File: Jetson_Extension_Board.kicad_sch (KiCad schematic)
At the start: 8 parts, among them J6 40_Pin_Jetson_Connector, SW1 SW_Push_DPDT

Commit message: PCB Update
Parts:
- added J14: Conn_01x06_Pin, Connector_JST:JST_EH_B6B-EH-A_1x06_P2.50mm_Vertical, symbol Connector:Conn_01x06_Pin
- added J15: Conn_01x04_Pin, Connector_JST:JST_EH_B4B-EH-A_1x04_P2.50mm_Vertical, symbol Connector:Conn_01x04_Pin
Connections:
- net 3.3V: now also SW1.3 (C); no longer SW1.1 (A)
- net ADC/3.3V: now also J14.5 (Pin_5), J14.6 (Pin_6)
- net COM 3: now also J15.1 (Pin_1)
- net GND: now also SW1.1 (A), J14.4 (Pin_4), J15.3 (Pin_3), J15.4 (Pin_4); no longer SW1.3 (C)
- net I2C_2_SCL: now also J14.2 (Pin_2)
- net I2C_2_SDA: now also J14.3 (Pin_3)
- net IMU INT: now also J15.2 (Pin_2)
- net IMU nRESET: now also J14.1 (Pin_1)
- net IMU nBOOT: no longer names the net of J6.33 (Pin_33)
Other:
- removed sheet IMU(BN0055)

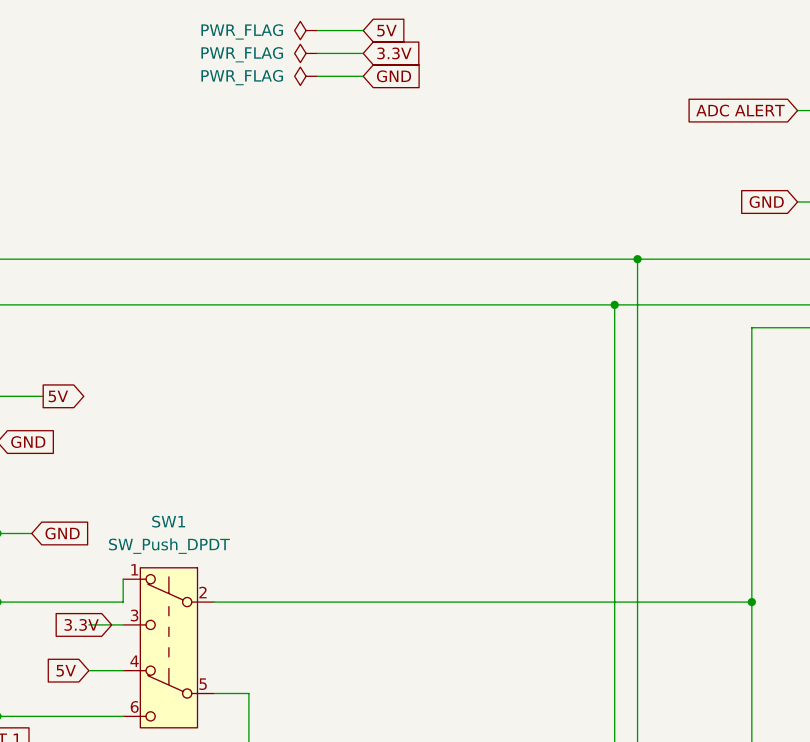
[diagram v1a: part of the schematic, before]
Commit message: added connectors for pots and compacted further
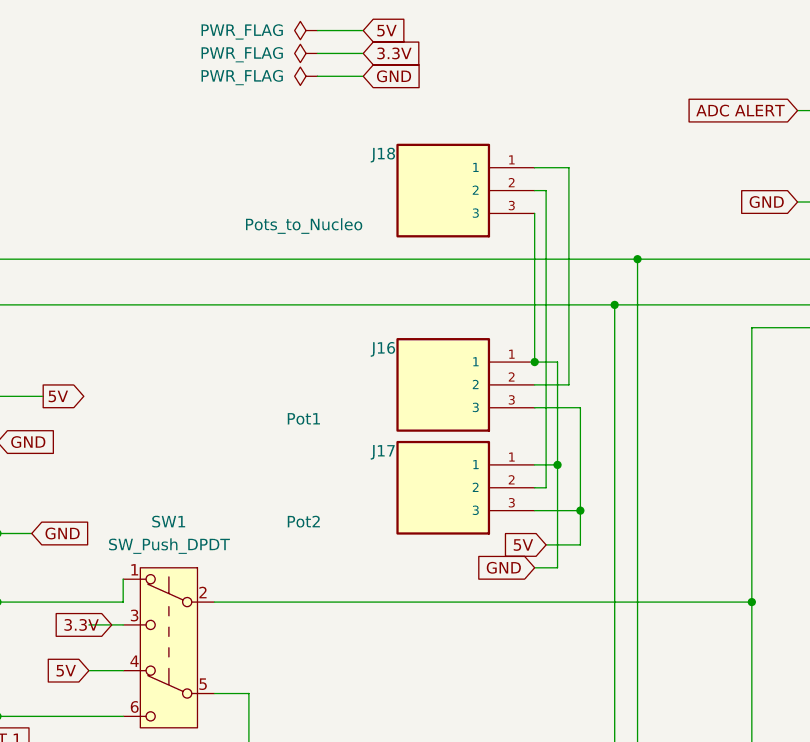
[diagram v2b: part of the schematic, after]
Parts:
- added J16: Pot1, TBP03R2_350_03BE(1):CUI_TBP03R2-350-03BE, symbol TBP03R2-350-03BE:TBP03R2-350-03BE
- added J17: Pot2, TBP03R2_350_03BE(1):CUI_TBP03R2-350-03BE, symbol TBP03R2-350-03BE:TBP03R2-350-03BE
- added J18: Pots_to_Nucleo, TBP03R2_350_03BE(1):CUI_TBP03R2-350-03BE, symbol TBP03R2-350-03BE:TBP03R2-350-03BE
- J14: footprint Connector_JST:JST_EH_B6B-EH-A_1x06_P2.50mm_Vertical -> Connector_PinSocket_2.54mm:PinSocket_1x06_P2.54mm_Vertical
- J15: footprint Connector_JST:JST_EH_B4B-EH-A_1x04_P2.50mm_Vertical -> Connector_PinSocket_2.54mm:PinSocket_1x04_P2.54mm_Vertical
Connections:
- net 5V: now also J16.3, J17.3
- net GND: now also J16.1, J17.1, J18.3
- new net: J17.2, J18.2
- new net: J16.2, J18.1

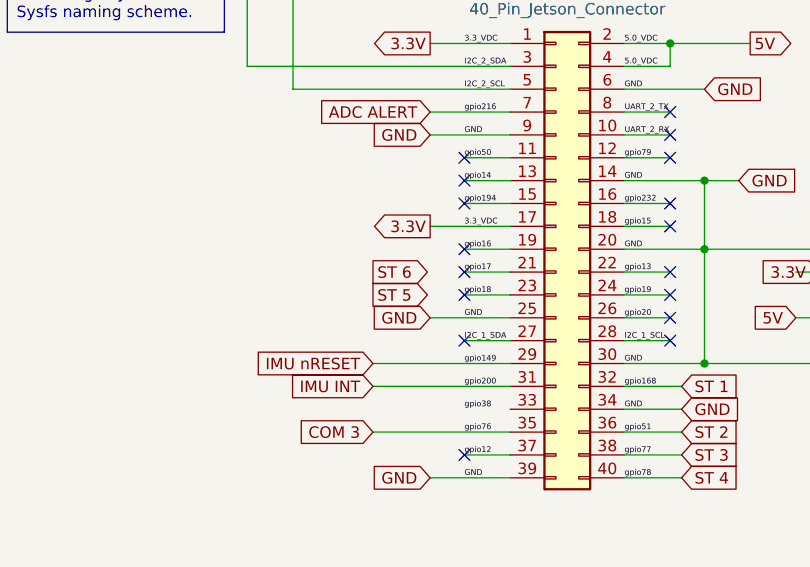
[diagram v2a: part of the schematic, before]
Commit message: changed hole sizes, added labels, added ground plane, set trace width min
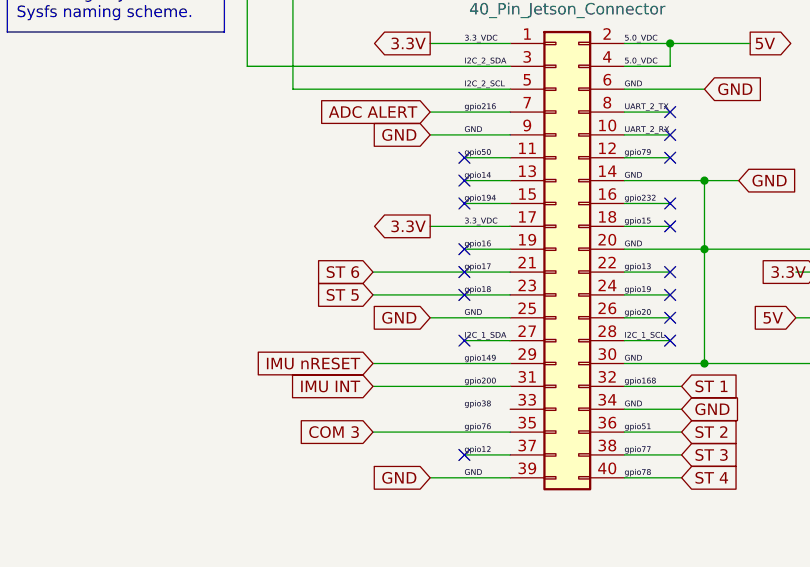
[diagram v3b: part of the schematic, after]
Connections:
- net gpio17 is gone; now on net ST 6: J6.21 (Pin_21)
- net gpio18 is gone; now on net ST 5: J6.23 (Pin_23)
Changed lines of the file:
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@@
+	(wire
+		(pts
+			(xy 57.15 99.06) (xy 72.39 99.06)
+		)
+		(stroke
+			(width 0)
+			(type default)
+		)
+	)
 	(wire
 		(pts
@@
 	(wire
 		(pts
-			(xy 67.31 101.6) (xy 72.39 101.6)
-		)
-		(stroke
-			(width 0)
-			(type default)
-		)
-	)
-	(wire
-		(pts
 			(xy 162.56 124.46) (xy 171.45 124.46)
 		)
@@
 	(wire
 		(pts
+			(xy 57.15 101.6) (xy 72.39 101.6)
+		)
+		(stroke
+			(width 0)
+			(type default)
+		)
+	)
+	(wire
+		(pts
 			(xy 48.26 63.5) (xy 48.26 78.74)
 		)
@@
 		(pts
 			(xy 153.67 53.34) (xy 153.67 69.85)
-		)
-		(stroke
-			(width 0)
-			(type default)
-		)
-	)
-	(wire
-		(pts
-			(xy 67.31 99.06) (xy 72.39 99.06)
 		)
 		(stroke
@@
 	)
 	(global_label "ST 5"
-		(shape output)
-		(at 57.15 101.6 0)
+		(shape input)
+		(at 57.15 101.6 180)
+		(fields_autoplaced yes)
+		(effects
+			(font
+				(size 1.27 1.27)
+			)
+			(justify right)
+		)
+		(property "Intersheetrefs" "${INTERSHEET_REFS}"
+			(at 49.8106 101.6 0)
+			(effects
+				(font
+					(size 1.27 1.27)
+				)
+				(justify right)
+				(hide yes)
+			)
+		)
+	)
+	(global_label "GND"
+		(shape input)
+		(at 93.98 78.74 0)
 		(fields_autoplaced yes)
 		(effects
@@
 		)
 		(property "Intersheetrefs" "${INTERSHEET_REFS}"
-			(at 64.4894 101.6 0)
+			(at 100.8357 78.74 0)
 			(effects
 				(font
@@
 		)
 	)
+	(global_label "ST 5"
+		(shape input)
+		(at 109.22 180.34 180)
+		(fields_autoplaced yes)
+		(effects
+			(font
+				(size 1.27 1.27)
+			)
+			(justify right)
+		)
+		(property "Intersheetrefs" "${INTERSHEET_REFS}"
+			(at 101.8806 180.34 0)
+			(effects
+				(font
+					(size 1.27 1.27)
+				)
+				(justify right)
+				(hide yes)
+			)
+		)
+	)
+	(global_label "ST 4"
+		(shape input)
+		(at 91.44 121.92 0)
+		(fields_autoplaced yes)
+		(effects
+			(font
+				(size 1.27 1.27)
+			)
+			(justify left)
+		)
+		(property "Intersheetrefs" "${INTERSHEET_REFS}"
+			(at 98.7794 121.92 0)
+			(effects
+				(font
+					(size 1.27 1.27)
+				)
+				(justify left)
+				(hide yes)
+			)
+		)
+	)
+	(global_label "3.3V"
+		(shape input)
+		(at 106.68 99.06 180)
+		(fields_autoplaced yes)
+		(effects
+			(font
+				(size 1.27 1.27)
+			)
+			(justify right)
+		)
+		(property "Intersheetrefs" "${INTERSHEET_REFS}"
+			(at 99.5824 99.06 0)
+			(effects
+				(font
+					(size 1.27 1.27)
+				)
+				(justify right)
+				(hide yes)
+			)
+		)
+	)
 	(global_label "GND"
 		(shape input)
-		(at 93.98 78.74 0)
-		(fields_autoplaced yes)
-		(effects
-			(font
-				(size 1.27 1.27)
-			)
-			(justify left)
-		)
-		(property "Intersheetrefs" "${INTERSHEET_REFS}"
-			(at 100.8357 78.74 0)
-			(effects
-				(font
-					(size 1.27 1.27)
-				)
-				(justify left)
-				(hide yes)
-			)
-		)
-	)
-	(global_label "ST 5"
-		(shape input)
-		(at 109.22 180.34 180)
-		(fields_autoplaced yes)
-		(effects
-			(font
-				(size 1.27 1.27)
-			)
-			(justify right)
-		)
-		(property "Intersheetrefs" "${INTERSHEET_REFS}"
-			(at 101.8806 180.34 0)
-			(effects
-				(font
-					(size 1.27 1.27)
-				)
-				(justify right)
-				(hide yes)
-			)
-		)
-	)
-	(global_label "ST 4"
-		(shape input)
-		(at 91.44 121.92 0)
-		(fields_autoplaced yes)
-		(effects
-			(font
-				(size 1.27 1.27)
-			)
-			(justify left)
-		)
-		(property "Intersheetrefs" "${INTERSHEET_REFS}"
-			(at 98.7794 121.92 0)
-			(effects
-				(font
-					(size 1.27 1.27)
-				)
-				(justify left)
-				(hide yes)
-			)
-		)
-	)
-	(global_label "3.3V"
-		(shape input)
-		(at 106.68 99.06 180)
-		(fields_autoplaced yes)
-		(effects
-			(font
-				(size 1.27 1.27)
-			)
-			(justify right)
-		)
-		(property "Intersheetrefs" "${INTERSHEET_REFS}"
-			(at 99.5824 99.06 0)
-			(effects
-				(font
-					(size 1.27 1.27)
-				)
-				(justify right)
-				(hide yes)
-			)
-		)
-	)
-	(global_label "GND"
-		(shape input)
 		(at 153.67 92.71 180)
 		(fields_autoplaced yes)
@@
 	)
 	(global_label "ST 6"
-		(shape output)
-		(at 57.15 99.06 0)
-		(fields_autoplaced yes)
-		(effects
-			(font
-				(size 1.27 1.27)
-			)
-			(justify left)
-		)
-		(property "Intersheetrefs" "${INTERSHEET_REFS}"
-			(at 64.4894 99.06 0)
-			(effects
-				(font
-					(size 1.27 1.27)
-				)
-				(justify left)
-				(hide yes)
-			)
+		(shape input)
+		(at 57.15 99.06 180)
+		(fields_autoplaced yes)
+		(effects
+			(font
+				(size 1.27 1.27)
+			)
+			(justify right)
+		)
+		(property "Intersheetrefs" "${INTERSHEET_REFS}"
+			(at 49.8106 99.06 0)
+			(effects
+				(font
+					(size 1.27 1.27)
+				)
+				(justify right)
+				(hide yes)
+			)
